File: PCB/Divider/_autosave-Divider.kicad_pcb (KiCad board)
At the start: 2 copper layers, 227.8 x 48 mm, 71 parts, among them J1 15kV, J2 10kV, J3 0V, J4 10kV, U1 SFH617A-1

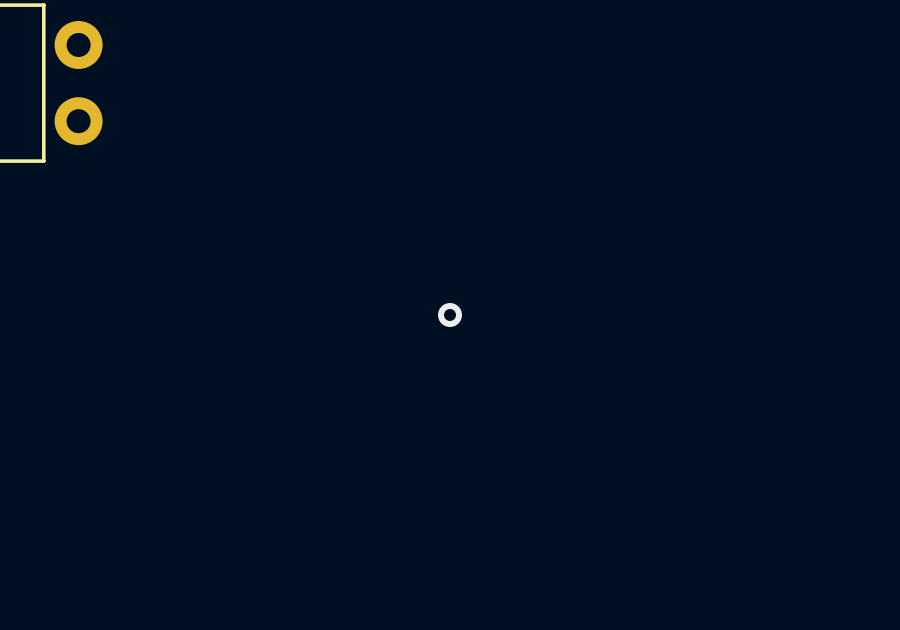
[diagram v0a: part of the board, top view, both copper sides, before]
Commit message: Begin PCB of divider
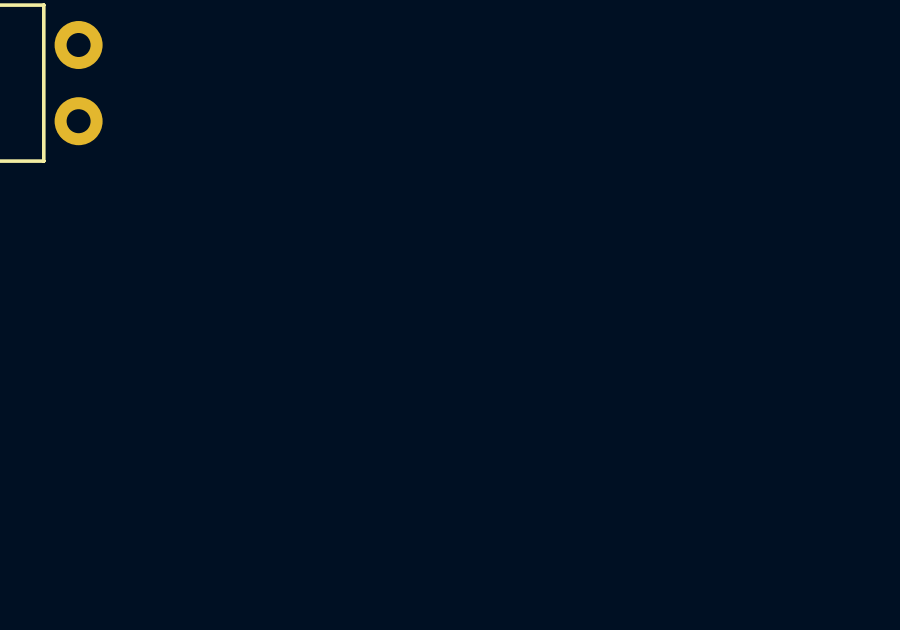
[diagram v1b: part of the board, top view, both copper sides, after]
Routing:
- net (no net): vias 1 -> 0
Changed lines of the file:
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@@
     (thickness 1.6)
     (drawings 13)
-    (tracks 1)
+    (tracks 0)
     (zones 0)
     (modules 71)
@@
   )
   (gr_line (start 152.8 52) (end 49 52) (layer Edge.Cuts) (width 0.05))
-  (via (at 240 69) (size 0.8) (drill 0.4) (layers F.Cu B.Cu) (net 0))
 )
